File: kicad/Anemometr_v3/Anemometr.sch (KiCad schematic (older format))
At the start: 136 parts, among them J1 TxD, J10 +Z1, J11 +Z2, J12 +Z3, J13 +Z4, J14 -Z1, J15 -Z2, J16 -Z3, J17 -Z4, J18 1 TxD+, J19 2 TxD-, J2 RxD, J20 3 RxD+, J21 4-5, J22 6 RxD-, J23 7-8, J24 +Z1, J25 +Z1, J26 +Z1, J27 +Z1, J28 +Z1, J29 +Z1, J3 SCL, J30 +Z1, J31 +Z1, J32 +Z1, J33 +Z1, J34 +Z1, J35 +Z1, J36 +Z1, J37 +Z1, J38 +Z1, J39 +Z1, J4 SDA, J5 RST, J6 +EXT, J7 -EXT, J8 SWD, J9 SWC, Q1 5N10, U1 STM32F103C8Tx, U4 LMR14206, U6 NCP1117-3.3, U9 MCP1703-3.3, Y1 CSTCE8M00G52A-R0, Y2 ECS-250-20-33

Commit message: изменено:      kicad/Anemometr_v3/Anemometr.kicad_pcb 	изменено:      kicad/Anemometr_v3/Anemometr.kicad_pcb-bak 	изменено:      kicad/Anemometr_v3/Anemometr.sch 	изменено:      kicad/Anemometr_v3/Anemometr.sch-bak
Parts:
- R15: footprint Resistor_SMD:R_0603_1608Metric -> Resistor_SMD:R_0402_1005Metric
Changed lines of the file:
@@
 F 0 "R15" V 9750 4950 50  0000 R CNN
 F 1 "4.7k" V 9850 4950 50  0000 R CNN
-F 2 "Resistor_SMD:R_0603_1608Metric" V 9880 4750 50  0001 C CNN
+F 2 "Resistor_SMD:R_0402_1005Metric" V 9880 4750 50  0001 C CNN
 F 3 "~" H 9950 4750 50  0001 C CNN
 	1    9950 4750

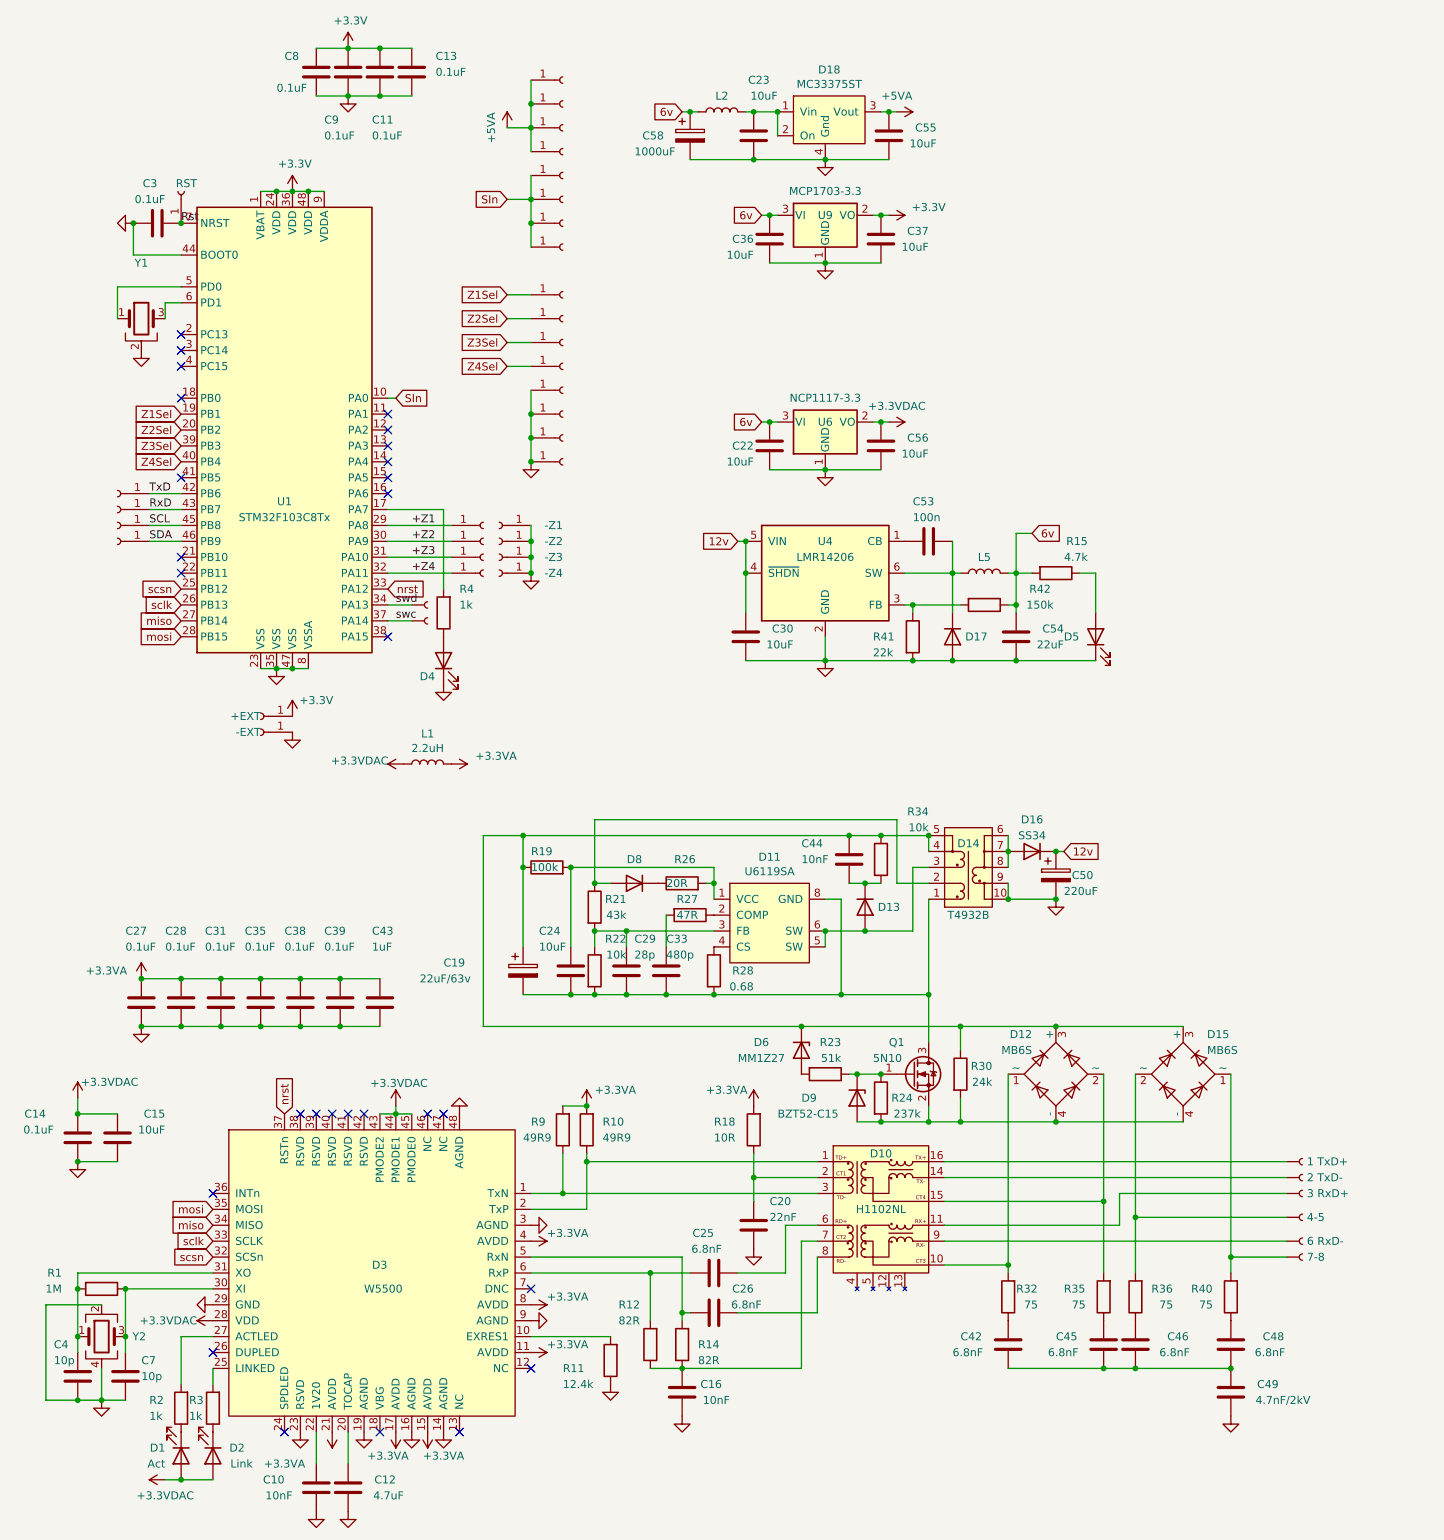
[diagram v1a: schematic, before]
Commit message: изменено:      kicad/Anemometr_v3/Anemometr-cache.lib 	изменено:      kicad/Anemometr_v3/Anemometr.kicad_pcb 	изменено:      kicad/Anemometr_v3/Anemometr.kicad_pcb-bak 	изменено:      kicad/Anemometr_v3/Anemometr.sch 	изменено:      kicad/Anemometr_v3/Anemometr.sch-bak 	изменено:      kicad/Anemometr_v3/fp-info-cache
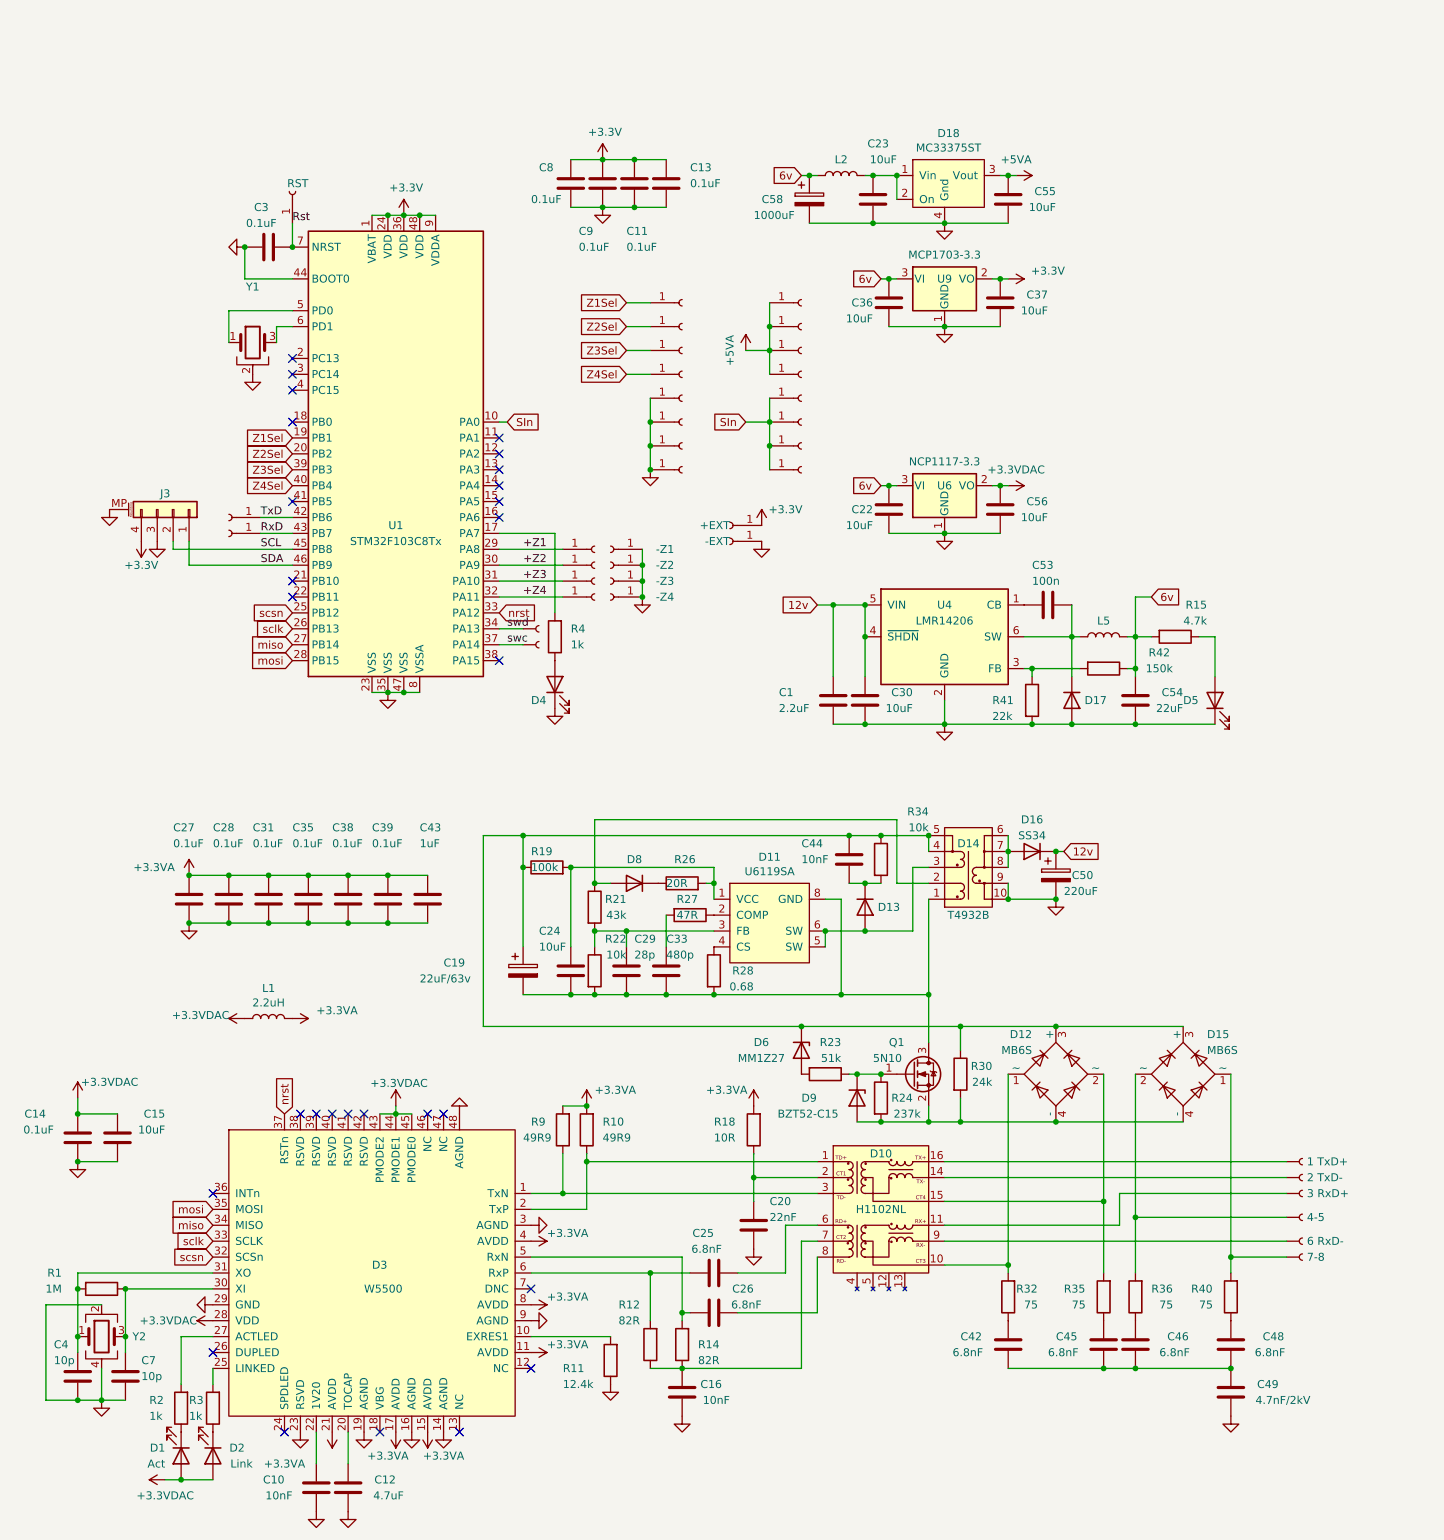
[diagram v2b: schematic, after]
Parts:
- removed J3: SCL, My-library:ConnMini, symbol Connector:Conn_01x01_Female
- removed J4: SDA, My-library:ConnMini, symbol Connector:Conn_01x01_Female
- added C1: 2.2uF, Capacitor_SMD:C_0603_1608Metric, symbol Device:C
- added J3: Conn_01x04_MountingPin, Connector_JST:JST_SH_BM04B-SRSS-TB_1x04-1MP_P1.00mm_Vertical, symbol Connector_Generic_MountingPin:Conn_01x04_MountingPin
- C56: footprint Capacitor_SMD:C_0805_2012Metric -> Capacitor_SMD:C_0603_1608Metric
- J10, J11, J12, J13, J28, J29, J30, J31, J32, J33, J34, J35: footprint My-library:SMD-CONN -> My-library:ConnMini
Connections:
- net +3V3: now also J3.4 (Pin_4)
- net 12v: now also C1.2
- net GND: now also C1.1, J3.3 (Pin_3), J3.MP (MountPin)
- net SCL: now also J3.2 (Pin_2)
- net SDA: now also J3.1 (Pin_1)
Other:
- moved on the sheet: C11, C13, C22, C23, C27, C28, C3, C30, C31, C35, C36, C37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

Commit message: изменено:      kicad/Anemometr_v3/Anemometr-cache.lib 	изменено:      kicad/Anemometr_v3/Anemometr.kicad_pcb 	изменено:      kicad/Anemometr_v3/Anemometr.kicad_pcb-bak 	изменено:      kicad/Anemometr_v3/Anemometr.sch 	изменено:      kicad/Anemometr_v3/Anemometr.sch-bak 	изменено:      kicad/Anemometr_v3/fp-info-cache
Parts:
- removed J18: 1 TxD+, My-library:SMD-CONN, symbol Anemometr-rescue:Conn-My_Library
- removed J19: 2 TxD-, My-library:SMD-CONN, symbol Anemometr-rescue:Conn-My_Library
- removed J20: 3 RxD+, My-library:SMD-CONN, symbol Anemometr-rescue:Conn-My_Library
- removed J21: 4-5, My-library:SMD-CONN, symbol Anemometr-rescue:Conn-My_Library
- removed J22: 6 RxD-, My-library:SMD-CONN, symbol Anemometr-rescue:Conn-My_Library
- removed J23: 7-8, My-library:SMD-CONN, symbol Anemometr-rescue:Conn-My_Library
- added J4: JST-SH1.0, Connector_JST:JST_SH_BM08B-SRSS-TB_1x08-1MP_P1.00mm_Vertical, symbol Connector_Generic_MountingPin:Conn_01x08_MountingPin
- C54: footprint Capacitor_SMD:C_1210_3225Metric -> Capacitor_SMD:C_0805_2012Metric
- D11: value U6119SA -> ?U6119SA?
- D14: value T4932B -> ?T4932B?
- J3: value Conn_01x04_MountingPin -> JST-SH1.0
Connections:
- net GND: now also J4.MP (MountPin)
- net at D10.10, R32.2: now also D12.2 (~~); no longer D12.1 (~~)
- net RxD+: now reaches D10.11
- net RxD+: now also J4.3 (Pin_3)
- net TxD-: now reaches D10.14
- net TxD-: now also J4.2 (Pin_2)
- net at D10.15, R35.2: now also D12.1 (~~); no longer D12.2 (~~)
- net TxD+: now reaches D10.16
- net TxD+: now also J4.1 (Pin_1)
- net RxD-: now reaches D10.9
- net RxD-: now also J4.4 (Pin_4)
- net 4-5: now reaches D15.2 (~~), R36.2
- net 4-5: now also J4.5 (Pin_5), J4.6 (Pin_6)
- net 7-8: now reaches D15.1 (~~), R40.2
- net 7-8: now also J4.7 (Pin_7), J4.8 (Pin_8)
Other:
- moved on the sheet: C1, C16, C20, C25, C26, C30, C36, C37, C53, C54, D17, D5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

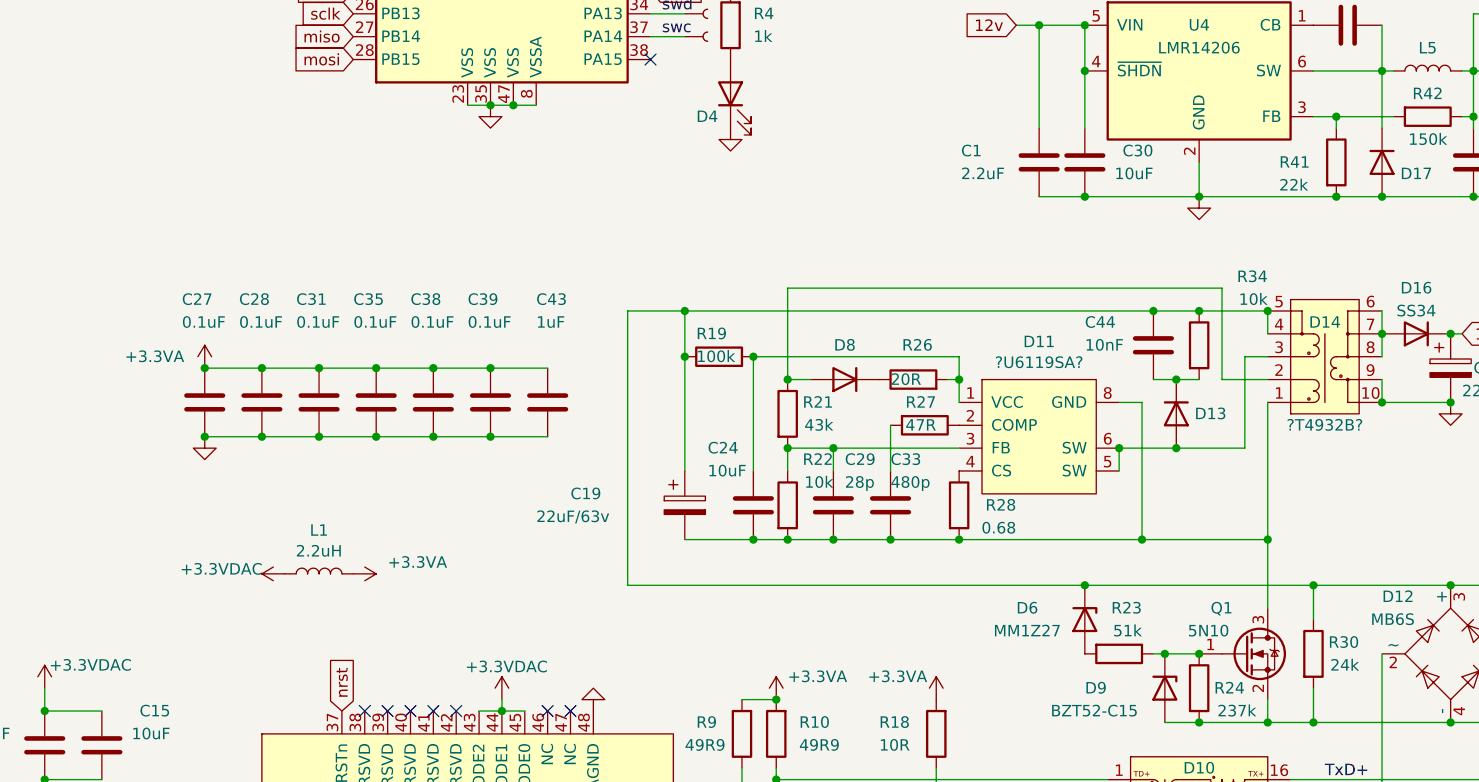
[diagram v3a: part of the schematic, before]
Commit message: изменено:      kicad/Anemometr_v3/Anemometr.kicad_pcb 	изменено:      kicad/Anemometr_v3/Anemometr.kicad_pcb-bak 	изменено:      kicad/Anemometr_v3/Anemometr.sch 	изменено:      kicad/Anemometr_v3/Anemometr.sch-bak 	изменено:      kicad/Anemometr_v3/fp-info-cache 	удалено:       stm32cubeide/Anemometr_v3/Anemometr_3 Debug.launch 	изменено:      stm32cubeide/Anemometr_v3/Anemometr_3.ioc 	изменено:      stm32cubeide/Anemometr_v3/Core/Inc/main.h 	изменено:      stm32cubeide/Anemometr_v3/Core/Src/main.c 	изменено:      stm32cubeide/Anemometr_v3/Core/Src/stm32f1xx_it.c 	изменено:      stm32cubeide/Anemometr_v3/Core/Src/wizchip_conf.c 	изменено:      stm32cubeide/Anemometr_v3/Debug/Anemometr_3.bin 	удалено:       stm32cubeide/Anemometr_v3/Debug/Anemometr_3.elf 	изменено:      stm32cubeide/Anemometr_v3/Debug/Anemometr_3.map 	изменено:      stm32cubeide/Anemometr_v3/Debug/Core/Src/BME280.d 	изменено:      stm32cubeide/Anemometr_v3/Debug/Core/Src/BME280.o 	изменено:      stm32cubeide/Anemometr_v3/Debug/Core/Src/main.d 	изменено:      stm32cubeide/Anemometr_v3/Debug/Core/Src/main.o 	изменено:      stm32cubeide/Anemometr_v3/Debug/Core/Src/main.su 	изменено:      stm32cubeide/Anemometr_v3/Debug/Core/Src/stm32f1xx_hal_msp.d 	изменено:      stm32cubeide/Anemometr_v3/Debug/Core/Src/stm32f1xx_hal_msp.o 	изменено:      stm32cubeide/Anemometr_v3/Debug/Core/Src/stm32f1xx_it.d 	изменено:      stm32cubeide/Anemometr_v3/Debug/Core/Src/stm32f1xx_it.o 	изменено:      stm32cubeide/Anemometr_v3/Debug/Core/Src/wizchip_conf.o 	изменено:      stm32cubeide/Anemometr_v3/Release/Anemometr_3.bin 	изменено:      stm32cubeide/Anemometr_v3/Release/Anemometr_3.elf 	изменено:      stm32cubeide/Anemometr_v3/Release/Anemometr_3.hex 	изменено:      stm32cubeide/Anemometr_v3/Release/Anemometr_3.list 	изменено:      stm32cubeide/Anemometr_v3/Release/Anemometr_3.map 	изменено:      stm32cubeide/Anemometr_v3/Release/Core/Src/BME280.d 	изменено:      stm32cubeide/Anemometr_v3/Release/Core/Src/BME280.o 	изменено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
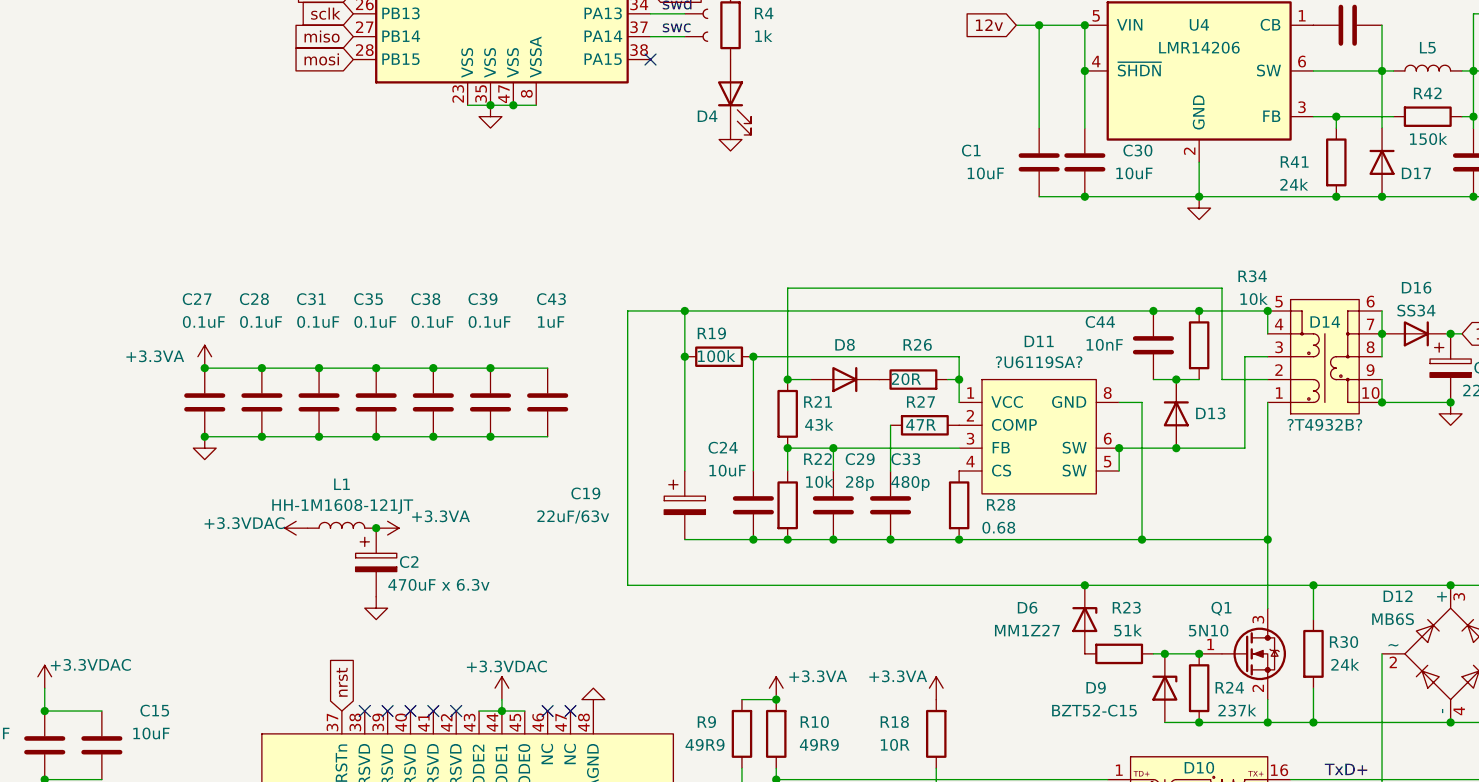
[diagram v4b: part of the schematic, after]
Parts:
- added C2: 470uF x 6.3v, Capacitor_Tantalum_SMD:CP_EIA-7343-15_Kemet-W, symbol Device:CP
- C1: value 2.2uF -> 10uF
- L1: value 2.2uH -> HH-1M1608-121JT; footprint Inductor_SMD:L_0805_2012Metric -> Inductor_SMD:L_0603_1608Metric
- R41: value 22k -> 24k
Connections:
- net +3.3VA: now also C2.1
- net GND: now also C2.2
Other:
- moved on the sheet: L1
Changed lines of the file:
@@
 L Device:L L1
 U 1 1 622C7BCA
-P 5000 7550
-F 0 "L1" V 5190 7550 50  0000 C CNN
-F 1 "2.2uH" V 5099 7550 50  0000 C CNN
-F 2 "Inductor_SMD:L_0805_2012Metric" H 5000 7550 50  0001 C CNN
-F 3 "~" H 5000 7550 50  0001 C CNN
-	1    5000 7550
+P 5100 7350
+F 0 "L1" V 5290 7350 50  0000 C CNN
+F 1 "HH-1M1608-121JT" V 5199 7350 50  0000 C CNN
+F 2 "Inductor_SMD:L_0603_1608Metric" H 5100 7350 50  0001 C CNN
+F 3 "~" H 5100 7350 50  0001 C CNN
+	1    5100 7350
 	0    -1   -1   0
 $EndComp
@@
 L power:+3.3VA #PWR031
 U 1 1 622CB3E8
-P 5150 7550
-F 0 "#PWR031" H 5150 7400 50  0001 C CNN
-F 1 "+3.3VA" V 5100 7700 50  0000 L CNN
-F 2 "" H 5150 7550 50  0001 C CNN
-F 3 "" H 5150 7550 50  0001 C CNN
-	1    5150 7550
+P 5250 7350
+F 0 "#PWR031" H 5250 7200 50  0001 C CNN
+F 1 "+3.3VA" V 5200 7500 50  0000 L CNN
+F 2 "" H 5250 7350 50  0001 C CNN
+F 3 "" H 5250 7350 50  0001 C CNN
+	1    5250 7350
 	0    1    1    0
 $EndComp
@@
 L power:+3.3VDAC #PWR025
 U 1 1 627337E2
-P 4850 7550
-F 0 "#PWR025" H 5000 7500 50  0001 C CNN
-F 1 "+3.3VDAC" V 4870 7647 50  0000 L CNN
-F 2 "" H 4850 7550 50  0001 C CNN
-F 3 "" H 4850 7550 50  0001 C CNN
-	1    4850 7550
+P 4950 7350
+F 0 "#PWR025" H 5100 7300 50  0001 C CNN
+F 1 "+3.3VDAC" V 4970 7447 50  0000 L CNN
+F 2 "" H 4950 7350 50  0001 C CNN
+F 3 "" H 4950 7350 50  0001 C CNN
+	1    4950 7350
 	0    -1   -1   0
 $EndComp
@@
 P 9450 5750
 F 0 "R41" H 9200 5750 50  0000 L CNN
-F 1 "22k" H 9200 5650 50  0000 L CNN
+F 1 "24k" H 9200 5650 50  0000 L CNN
 F 2 "Resistor_SMD:R_0603_1608Metric" V 9380 5750 50  0001 C CNN
 F 3 "~" H 9450 5750 50  0001 C CNN
@@
 P 8150 5750
 F 0 "C1" H 8400 5700 50  0000 L CNN
-F 1 "2.2uF" H 8300 5800 50  0000 L CNN
+F 1 "10uF" H 8300 5800 50  0000 L CNN
 F 2 "Capacitor_SMD:C_0603_1608Metric" H 8188 5600 50  0001 C CNN
 F 3 "~" H 8150 5750 50  0001 C CNN
@@
 	11550 8950 11550 8850
 Connection ~ 11550 8850
+$Comp
+L Device:CP C2
+U 1 1 640E201E
+P 5250 7500
+F 0 "C2" H 5350 7500 50  0000 L CNN
+F 1 "470uF x 6.3v" H 5300 7400 50  0000 L CNN
+F 2 "Capacitor_Tantalum_SMD:CP_EIA-7343-15_Kemet-W" H 5288 7350 50  0001 C CNN
+F 3 "~" H 5250 7500 50  0001 C CNN
+	1    5250 7500
+	1    0    0    -1
+$EndComp
+Connection ~ 5250 7350
+$Comp
+L power:GND #PWR029
+U 1 1 64107A1E
+P 5250 7650
+F 0 "#PWR029" H 5250 7400 50  0001 C CNN
+F 1 "GND" H 5255 7477 50  0001 C CNN
+F 2 "" H 5250 7650 50  0001 C CNN
+F 3 "" H 5250 7650 50  0001 C CNN
+	1    5250 7650
+	1    0    0    -1
+$EndComp
 $EndSCHEMATC
